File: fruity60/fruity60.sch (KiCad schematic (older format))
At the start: 126 parts

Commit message: Add footprints
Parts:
- D1, D10, D11, D12, D13, D14, D15, D16, D17, D18, D19, D2, D20, D21, D22, D23, D24, D25, D26, D27, D28, D29, D3, D30, D31, D32, D33, D34, D35, D36, D37, D38, D39, D4, D40, D41, D42, D43, D44, D45, D46, D47, D48, D49, D5, D50, D51, D52, D53, D54, D55, D56, D57, D58, D59, D6, D60, D61, D62, D7, D8, D9: footprint (none) -> Diodes_SMD:D_SOD-123
- JP1: footprint Untitled:1X16_ROUND -> Pin_Headers:Pin_Header_Angled_1x16_Pitch1.00mm
- JP2: footprint Untitled:1X12_ROUND -> Pin_Headers:Pin_Header_Angled_1x12_Pitch1.00mm
- MX1, MX10, MX11, MX12, MX13, MX14, MX15, MX16, MX18, MX19, MX20, MX21, MX22, MX23, MX24, MX25, MX26, MX27, MX28, MX29, MX30, MX31, MX32, MX35, MX36, MX37, MX38, MX39, MX40, MX41, MX42, MX43, MX45, MX46, MX47, MX48, MX51, MX52, MX53, MX54, MX55, MX56, MX57, MX58, MX59, MX6, MX60, MX61, MX7, MX8, MX9: footprint (none) -> MX_Only:MXOnly-1U
- MX17, MX2, MX34, MX49, MX5, MX62: footprint (none) -> MX_Only:MXOnly-1.5U
- MX3, MX50: footprint (none) -> MX_Only:MXOnly-1.75U
- MX33: footprint (none) -> MX_Only:MXOnly-7U
- MX4, MX44: footprint (none) -> MX_Only:MXOnly-2.25U

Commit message: fix up key sizes
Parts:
- MX55: renamed from MX34; footprint MX_Only:MXOnly-1.5U -> MX_Only:MXOnly-1U
- MX56: renamed from MX39; footprint MX_Only:MXOnly-1U -> MX_Only:MXOnly-1.5U
- MX57: renamed from MX44; footprint MX_Only:MXOnly-2.25U -> MX_Only:MXOnly-1U
- MX58: renamed from MX50; footprint MX_Only:MXOnly-1.75U -> MX_Only:MXOnly-2.25U
- MX59: renamed from MX56; footprint MX_Only:MXOnly-1U -> MX_Only:MXOnly-1.75U
- MX5A1: renamed from MX62; footprint MX_Only:MXOnly-1.5U -> MX_Only:MXOnly-1U
- renumbered MX1 to MX0, MX57 to MX0A1, MX7 to MX1, MX2 to MX10, MX8 to MX11, MX14 to MX12, MX20 to MX13, MX25 to MX14, MX30 to MX15, MX36 to MX16, MX41 to MX17, MX46 to MX18, MX52 to MX19, MX58 to MX1A1, MX13 to MX2, MX3 to MX20, MX9 to MX21, MX15 to MX22, MX21 to MX23, MX26 to MX24, MX31 to MX25, MX37 to MX26, MX42 to MX27, MX47 to MX28, MX53 to MX29, MX59 to MX2A1, MX19 to MX3, MX4 to MX30, MX10 to MX31, MX16 to MX32, MX22 to MX33, MX27 to MX34, MX32 to MX35, MX38 to MX36, MX43 to MX37, MX48 to MX38, MX54 to MX39, MX60 to MX3A1, MX24 to MX4, MX5 to MX40, MX11 to MX41, MX17 to MX42, MX33 to MX45, MX49 to MX48, MX55 to MX49, MX61 to MX4A, MX29 to MX5, MX6 to MX50, MX12 to MX51, MX18 to MX52, MX23 to MX53, MX28 to MX54, MX35 to MX6, MX40 to MX7, MX45 to MX8, MX51 to MX9

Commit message: Basic layout of switches
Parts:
- MX4A1: renamed from MX4A; footprint MX_Only:MXOnly-1U -> MX_Only:MXOnly-1.5U
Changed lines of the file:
@@
 	5800 6700 5700 6700
 $Comp
-L MX_Alps_Hybrid:MX-NoLED MX4A
+L MX_Alps_Hybrid:MX-NoLED MX4A1
 U 1 1 5DC0DBE6
 P 6350 6550
-F 0 "MX4A" H 6383 6773 60  0000 C CNN
+F 0 "MX4A1" H 6383 6773 60  0000 C CNN
 F 1 "MX-NoLED" H 6383 6699 20  0000 C CNN
-F 2 "MX_Only:MXOnly-1U" H 5725 6525 60  0001 C CNN
+F 2 "MX_Only:MXOnly-1.5U" H 5725 6525 60  0001 C CNN
 F 3 "" H 5725 6525 60  0001 C CNN
 	1    6350 6550

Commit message: flip diodes. Thanks Skully
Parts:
- renumbered D1 to D0, D7 to D1, D2 to D10, D8 to D11, D14 to D12, D20 to D13, D25 to D14, D30 to D15, D36 to D16, D41 to D17, D46 to D18, D52 to D19, D58 to D1A1, D13 to D2, D3 to D20, D9 to D21, D15 to D22, D21 to D23, D26 to D24, D31 to D25, D37 to D26, D42 to D27, D47 to D28, D53 to D29, D59 to D2A1, D19 to D3, D4 to D30, D10 to D31, D16 to D32, D22 to D33, D27 to D34, D32 to D35, D38 to D36, D43 to D37, D48 to D38, D54 to D39, D60 to D3A1, D24 to D4, D5 to D40, D11 to D41, D17 to D42, D33 to D45, D49 to D48, D55 to D49, D61 to D4A1, D29 to D5, D6 to D50, D12 to D51, D18 to D52, D23 to D53, D28 to D54, D34 to D55, D39 to D56, D44 to D57, D50 to D58, D56 to D59, D62 to D5A1, D35 to D6, D40 to D7, D45 to D8, D51 to D9, D57 to DA1

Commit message: Use 2.54 straight headers not angled
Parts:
- JP1: footprint Pin_Headers:Pin_Header_Angled_1x16_Pitch1.00mm -> Pin_Headers:Pin_Header_Straight_1x16_Pitch2.54mm
- JP2: footprint Pin_Headers:Pin_Header_Angled_1x12_Pitch1.00mm -> Pin_Headers:Pin_Header_Straight_1x11_Pitch2.54mm
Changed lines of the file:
@@
 F 0 "JP1" H 7000 2675 59  0000 L BNN
 F 1 "HEADER-1X16ROUND" H 7000 850 59  0000 L BNN
-F 2 "Pin_Headers:Pin_Header_Angled_1x16_Pitch1.00mm" H 7250 1850 50  0001 C CNN
+F 2 "Pin_Headers:Pin_Header_Straight_1x16_Pitch2.54mm" H 7250 1850 50  0001 C CNN
 F 3 "" H 7250 1850 50  0001 C CNN
 	1    7250 1850
@@
 F 0 "JP2" H 8800 5625 59  0000 L BNN
 F 1 "HEADER-1X12" H 8800 4200 59  0000 L BNN
-F 2 "Pin_Headers:Pin_Header_Angled_1x12_Pitch1.00mm" H 9050 4900 50  0001 C CNN
+F 2 "Pin_Headers:Pin_Header_Straight_1x11_Pitch2.54mm" H 9050 4900 50  0001 C CNN
 F 3 "" H 9050 4900 50  0001 C CNN
 	1    9050 4900

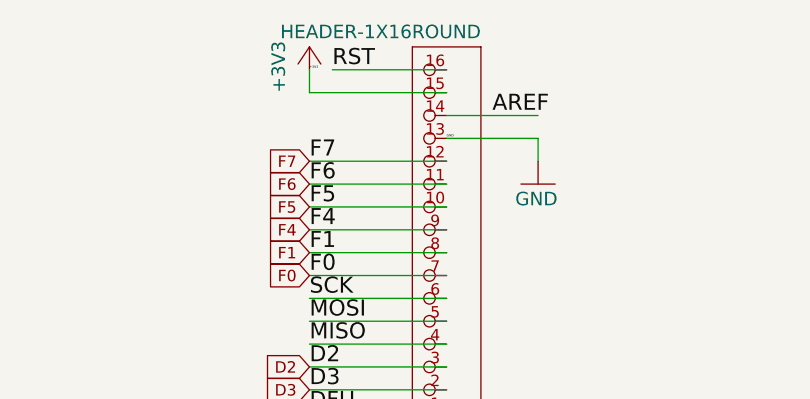
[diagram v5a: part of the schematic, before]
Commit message: Routing weirdness
 May need to change footprint for diodes
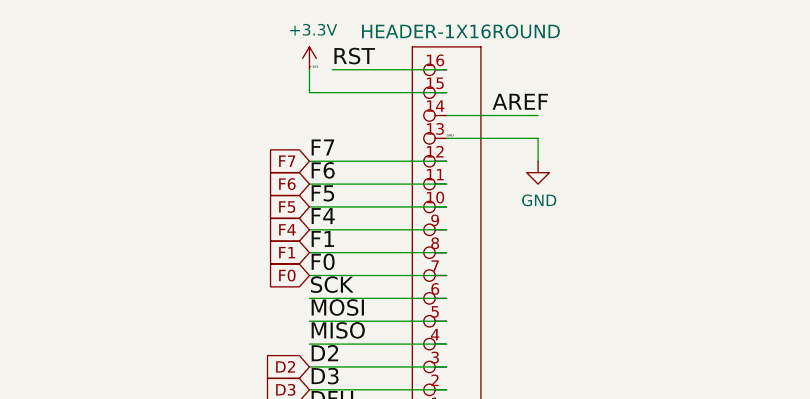
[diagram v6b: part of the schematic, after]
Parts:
- JP2: footprint Pin_Headers:Pin_Header_Straight_1x11_Pitch2.54mm -> Pin_Headers:Pin_Header_Straight_1x12_Pitch2.54mm
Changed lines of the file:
@@
 P 7250 1850
 F 0 "JP1" H 7000 2675 59  0000 L BNN
-F 1 "HEADER-1X16ROUND" H 7000 850 59  0000 L BNN
+F 1 "HEADER-1X16ROUND" H 6650 850 59  0000 L BNN
 F 2 "Pin_Headers:Pin_Header_Straight_1x16_Pitch2.54mm" H 7250 1850 50  0001 C CNN
 F 3 "" H 7250 1850 50  0001 C CNN
 	1    7250 1850
 	-1   0    0    1
-$EndComp
-$Comp
-L Untitled-eagle-import:+3V3 #+3V0101
-U 1 1 612E3AAF
-P 6750 950
-F 0 "#+3V0101" H 6750 950 50  0001 C CNN
-F 1 "+3V3" V 6650 750 59  0000 L BNN
-F 2 "" H 6750 950 50  0001 C CNN
-F 3 "" H 6750 950 50  0001 C CNN
-	1    6750 950
-	1    0    0    -1
-$EndComp
-$Comp
-L Untitled-eagle-import:GND #GND0101
-U 1 1 6AE2E73F
-P 7750 1550
-F 0 "#GND0101" H 7750 1550 50  0001 C CNN
-F 1 "GND" H 7650 1450 59  0000 L BNN
-F 2 "" H 7750 1550 50  0001 C CNN
-F 3 "" H 7750 1550 50  0001 C CNN
-	1    7750 1550
-	1    0    0    -1
 $EndComp
 $Comp
@@
 F 0 "JP2" H 8800 5625 59  0000 L BNN
 F 1 "HEADER-1X12" H 8800 4200 59  0000 L BNN
-F 2 "Pin_Headers:Pin_Header_Straight_1x11_Pitch2.54mm" H 9050 4900 50  0001 C CNN
+F 2 "Pin_Headers:Pin_Header_Straight_1x12_Pitch2.54mm" H 9050 4900 50  0001 C CNN
 F 3 "" H 9050 4900 50  0001 C CNN
 	1    9050 4900
@@
 	6200 7650 6650 7650
 Connection ~ 6200 7650
-Text GLabel 8050 5400 0    50   Input ~ 0
-D1
+Text GLabel 8050 4900 0    50   Input ~ 0
+B6
 Text GLabel 6650 7650 2    50   Input ~ 0
 D1
 Text GLabel 6650 6900 2    50   Input ~ 0
 D0
-Text GLabel 8050 5300 0    50   Input ~ 0
-D0
+Text GLabel 8050 5000 0    50   Input ~ 0
+B5
+Text GLabel 8050 5100 0    50   Input ~ 0
+D7
 Text GLabel 8050 5200 0    50   Input ~ 0
 C6
-Text GLabel 8050 5100 0    50   Input ~ 0
-D7
 Text GLabel 6950 6100 2    50   Input ~ 0
 C6
@@
 Text GLabel 6900 3900 2    50   Input ~ 0
 B6
-Text GLabel 8050 5000 0    50   Input ~ 0
-B5
-Text GLabel 8050 4900 0    50   Input ~ 0
-B6
+Text GLabel 8050 5300 0    50   Input ~ 0
+D0
+Text GLabel 8050 5400 0    50   Input ~ 0
+D1
 Connection ~ 3900 5700
 Wire Wire Line
@@
 	0    -1   -1   0
 $EndComp
+$Comp
+L power:+3.3V #PWR0101
+U 1 1 5D973091
+P 6750 1050
+F 0 "#PWR0101" H 6750 900 50  0001 C CNN
+F 1 "+3.3V" H 6765 1223 50  0000 C CNN
+F 2 "" H 6750 1050 50  0001 C CNN
+F 3 "" H 6750 1050 50  0001 C CNN
+	1    6750 1050
+	1    0    0    -1
+$EndComp
+$Comp
+L power:GND #PWR0102
+U 1 1 5D983D3C
+P 7750 1450
+F 0 "#PWR0102" H 7750 1200 50  0001 C CNN
+F 1 "GND" H 7755 1277 50  0000 C CNN
+F 2 "" H 7750 1450 50  0001 C CNN
+F 3 "" H 7750 1450 50  0001 C CNN
+	1    7750 1450
+	1    0    0    -1
+$EndComp
 $EndSCHEMATC

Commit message: progress
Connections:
- net B7: now also MX18.1 (COL), MX28.1 (COL), MX38.1 (COL), MX48.1 (COL), MX58.1 (COL), MX8.1 (COL); no longer MX0A1.1 (COL), MX1A1.1 (COL), MX2A1.1 (COL), MX3A1.1 (COL), MX4A1.1 (COL), MX5A1.1 (COL)
- net C7: now also MX0A1.1 (COL), MX1A1.1 (COL), MX2A1.1 (COL), MX3A1.1 (COL), MX4A1.1 (COL), MX5A1.1 (COL); no longer MX18.1 (COL), MX28.1 (COL), MX38.1 (COL), MX48.1 (COL), MX58.1 (COL), MX8.1 (COL)
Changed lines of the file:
@@
 Text GLabel 6750 2450 0    50   Input ~ 0
 D3
-Text GLabel 8050 4600 0    50   Input ~ 0
-C7
 Text GLabel 8050 4700 0    50   Input ~ 0
 D6
@@
 D3
 Text GLabel 5500 3050 1    50   Input ~ 0
-C7
+B7
 Text GLabel 6000 3050 1    50   Input ~ 0
 D6
 Text GLabel 6500 3000 1    50   Input ~ 0
-B7
+C7
 $Comp
 L Device:D_Small D5
@@
 	1    0    0    -1
 $EndComp
+Text GLabel 8050 4600 0    50   Input ~ 0
+C7
 $EndSCHEMATC

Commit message: Update with all nets
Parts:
- JP1: footprint Pin_Headers:Pin_Header_Straight_1x16_Pitch2.54mm -> Adafruit Feather 32u4 Bluefruit LE:1X16_ROUND
- JP2: footprint Pin_Headers:Pin_Header_Straight_1x12_Pitch2.54mm -> Adafruit Feather 32u4 Bluefruit LE:1X12_ROUND
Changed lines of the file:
@@
 F 0 "JP1" H 7000 2675 59  0000 L BNN
 F 1 "HEADER-1X16ROUND" H 6650 850 59  0000 L BNN
-F 2 "Pin_Headers:Pin_Header_Straight_1x16_Pitch2.54mm" H 7250 1850 50  0001 C CNN
+F 2 "Adafruit Feather 32u4 Bluefruit LE:1X16_ROUND" H 7250 1850 50  0001 C CNN
 F 3 "" H 7250 1850 50  0001 C CNN
 	1    7250 1850
@@
 F 0 "JP2" H 8800 5625 59  0000 L BNN
 F 1 "HEADER-1X12" H 8800 4200 59  0000 L BNN
-F 2 "Pin_Headers:Pin_Header_Straight_1x12_Pitch2.54mm" H 9050 4900 50  0001 C CNN
+F 2 "Adafruit Feather 32u4 Bluefruit LE:1X12_ROUND" H 9050 4900 50  0001 C CNN
 F 3 "" H 9050 4900 50  0001 C CNN
 	1    9050 4900
